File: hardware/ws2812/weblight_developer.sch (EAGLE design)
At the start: 14 parts, among them U1 ATTiny85-20SU

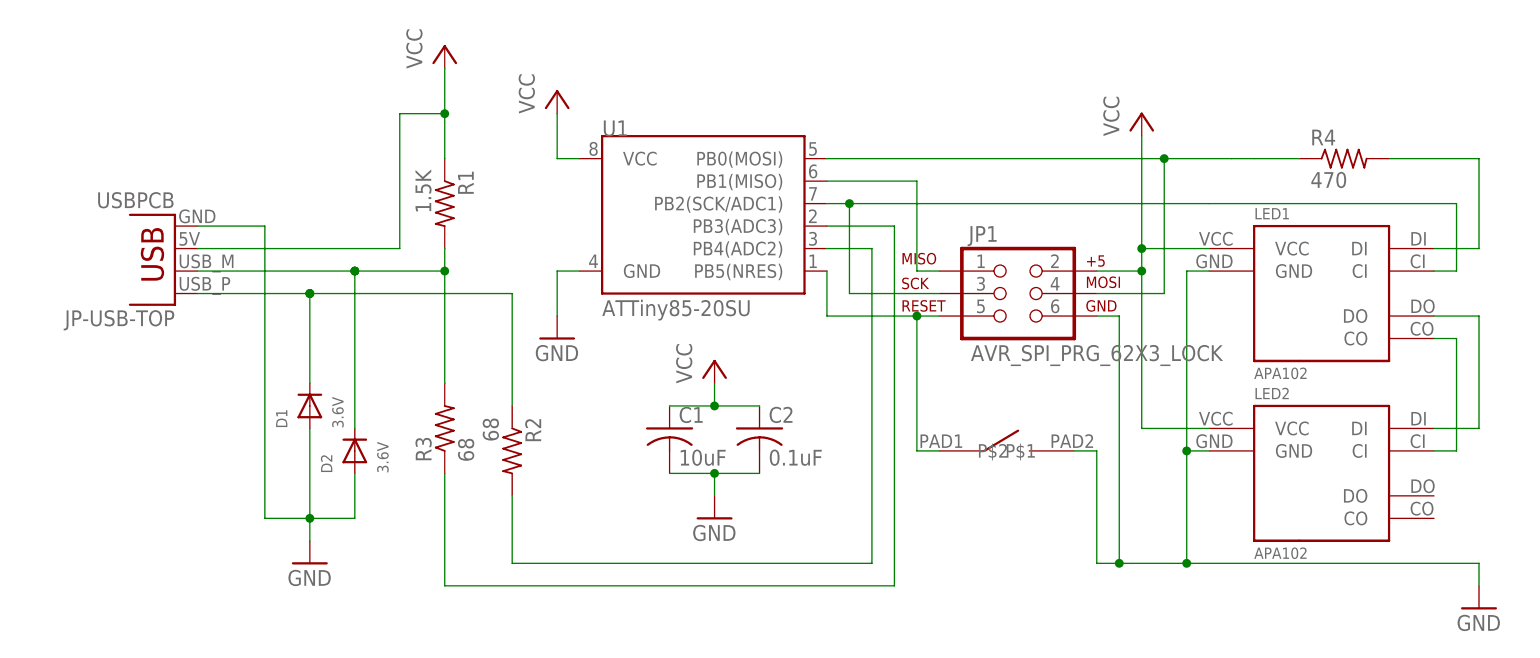
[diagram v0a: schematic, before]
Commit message: Separate LED type and adopt new board versioning scheme
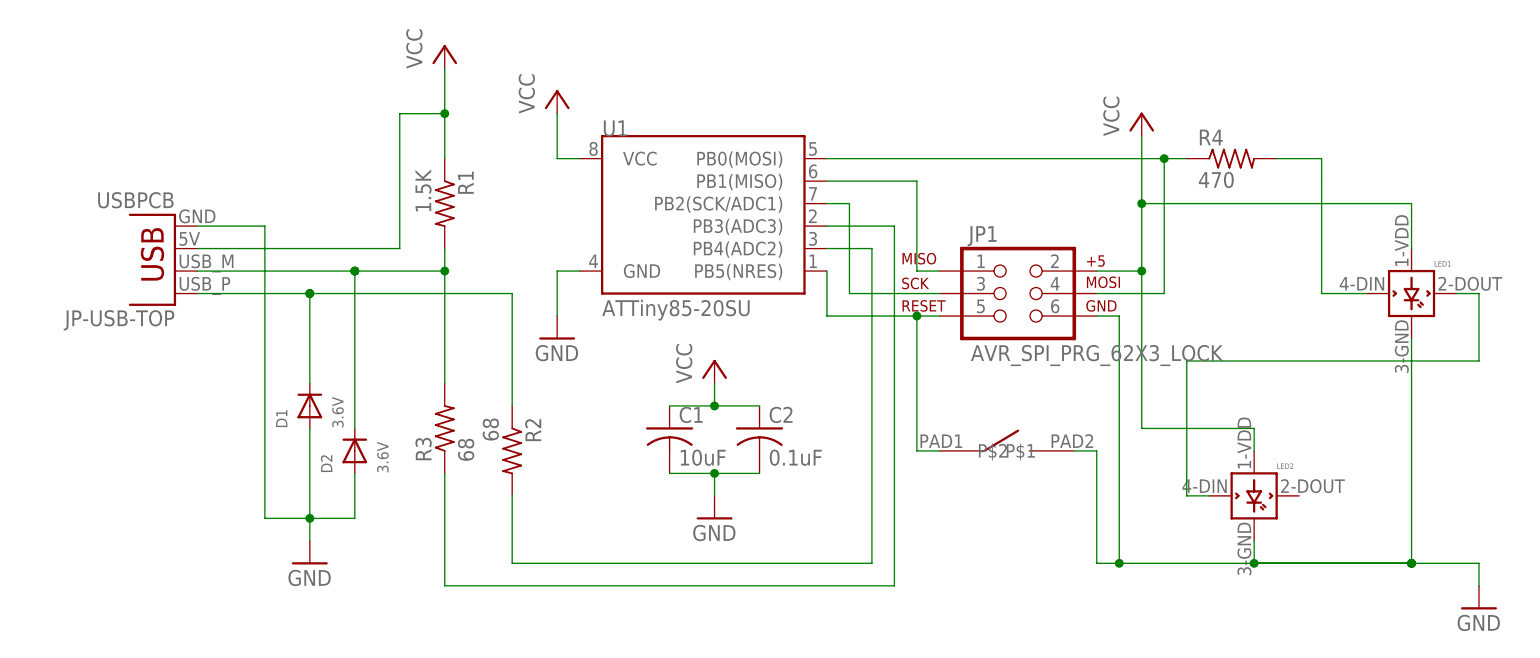
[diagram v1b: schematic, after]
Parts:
- LED1, LED2: value APA102 -> WS2812B; device weblight:APA102 -> weblight:WS2812B
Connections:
- removed net SCK_1: JP1.3, LED1.CI, U1.PB2(SCK/ADC1)
- removed net SCK_2: LED1.CO, LED2.CI
- new net N$4: JP1.3, U1.PB2(SCK/ADC1)
- net DIN_1: now also LED1.DIN; no longer LED1.DI
- net DIN_2: now also LED1.DOUT, LED2.DIN; no longer LED1.DO, LED2.DI
- net VCC: now also LED1.VDD, LED2.VDD; no longer LED1.VCC, LED2.VCC
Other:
- moved on the sheet: R4
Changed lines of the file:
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@@
 <part name="JP1" library="SparkFun-Connectors" deviceset="AVR_SPI_PRG_6" device="2X3_LOCK"/>
 <part name="SW_RESET" library="weblight" deviceset="BUTTON_TD-85XU" device=""/>
-<part name="LED1" library="weblight" deviceset="APA102" device=""/>
-<part name="LED2" library="weblight" deviceset="APA102" device=""/>
+<part name="LED1" library="weblight" deviceset="WS2812B" device=""/>
+<part name="LED2" library="weblight" deviceset="WS2812B" device=""/>
 </parts>
 <sheets>
@@
 <instance part="GND4" gate="1" x="99.06" y="30.48"/>
 <instance part="P+5" gate="VCC" x="60.96" y="86.36"/>
-<instance part="R4" gate="G$1" x="83.82" y="81.28"/>
+<instance part="R4" gate="G$1" x="71.12" y="81.28"/>
 <instance part="JP1" gate="G$1" x="45.72" y="66.04"/>
 <instance part="SW_RESET" gate="G$1" x="45.72" y="48.26"/>
-<instance part="LED1" gate="G$1" x="81.28" y="63.5"/>
-<instance part="LED2" gate="G$1" x="81.28" y="43.18"/>
+<instance part="LED1" gate="G$1" x="91.44" y="66.04"/>
+<instance part="LED2" gate="G$1" x="73.66" y="43.18"/>
 </instances>
 <busses>
@@
 </segment>
 <segment>
-<wire x1="60.96" y1="71.12" x2="68.58" y2="71.12" width="0.1524" layer="91"/>
 <pinref part="P+5" gate="VCC" pin="VCC"/>
 <wire x1="60.96" y1="50.8" x2="60.96" y2="68.58" width="0.1524" layer="91"/>
-<wire x1="60.96" y1="68.58" x2="60.96" y2="71.12" width="0.1524" layer="91"/>
-<wire x1="60.96" y1="83.82" x2="60.96" y2="71.12" width="0.1524" layer="91"/>
-<junction x="60.96" y="71.12"/>
+<wire x1="60.96" y1="68.58" x2="60.96" y2="76.2" width="0.1524" layer="91"/>
+<wire x1="60.96" y1="83.82" x2="60.96" y2="76.2" width="0.1524" layer="91"/>
 <pinref part="JP1" gate="G$1" pin="2"/>
 <wire x1="55.88" y1="68.58" x2="60.96" y2="68.58" width="0.1524" layer="91"/>
 <junction x="60.96" y="68.58"/>
-<pinref part="LED1" gate="G$1" pin="VCC"/>
-<pinref part="LED2" gate="G$1" pin="VCC"/>
-<wire x1="60.96" y1="50.8" x2="68.58" y2="50.8" width="0.1524" layer="91"/>
+<wire x1="60.96" y1="50.8" x2="73.66" y2="50.8" width="0.1524" layer="91"/>
+<pinref part="LED2" gate="G$1" pin="VDD"/>
+<wire x1="73.66" y1="50.8" x2="73.66" y2="48.26" width="0.1524" layer="91"/>
+<pinref part="LED1" gate="G$1" pin="VDD"/>
+<wire x1="91.44" y1="76.2" x2="91.44" y2="71.12" width="0.1524" layer="91"/>
+<wire x1="91.44" y1="76.2" x2="60.96" y2="76.2" width="0.1524" layer="91"/>
+<junction x="60.96" y="76.2"/>
 </segment>
 </net>
@@
 <pinref part="GND4" gate="1" pin="GND"/>
 <wire x1="99.06" y1="35.56" x2="99.06" y2="33.02" width="0.1524" layer="91"/>
-<wire x1="99.06" y1="35.56" x2="66.04" y2="35.56" width="0.1524" layer="91"/>
-<wire x1="66.04" y1="35.56" x2="58.42" y2="35.56" width="0.1524" layer="91"/>
+<wire x1="99.06" y1="35.56" x2="91.44" y2="35.56" width="0.1524" layer="91"/>
+<wire x1="91.44" y1="35.56" x2="73.66" y2="35.56" width="0.1524" layer="91"/>
+<wire x1="73.66" y1="35.56" x2="91.44" y2="35.56" width="0.1524" layer="91"/>
+<wire x1="91.44" y1="35.56" x2="73.66" y2="35.56" width="0.1524" layer="91"/>
+<wire x1="73.66" y1="35.56" x2="58.42" y2="35.56" width="0.1524" layer="91"/>
 <wire x1="58.42" y1="35.56" x2="58.42" y2="63.5" width="0.1524" layer="91"/>
 <pinref part="JP1" gate="G$1" pin="6"/>
@@
 <wire x1="55.88" y1="35.56" x2="58.42" y2="35.56" width="0.1524" layer="91"/>
 <junction x="58.42" y="35.56"/>
+<junction x="91.44" y="35.56"/>
+<junction x="91.44" y="35.56"/>
 <pinref part="LED1" gate="G$1" pin="GND"/>
-<wire x1="68.58" y1="68.58" x2="66.04" y2="68.58" width="0.1524" layer="91"/>
-<wire x1="66.04" y1="68.58" x2="66.04" y2="48.26" width="0.1524" layer="91"/>
-<junction x="66.04" y="35.56"/>
+<wire x1="91.44" y1="35.56" x2="91.44" y2="60.96" width="0.1524" layer="91"/>
 <pinref part="LED2" gate="G$1" pin="GND"/>
-<wire x1="66.04" y1="48.26" x2="66.04" y2="35.56" width="0.1524" layer="91"/>
-<wire x1="66.04" y1="48.26" x2="68.58" y2="48.26" width="0.1524" layer="91"/>
-<junction x="66.04" y="48.26"/>
+<wire x1="73.66" y1="35.56" x2="73.66" y2="38.1" width="0.1524" layer="91"/>
+<junction x="73.66" y="35.56"/>
 </segment>
 <segment>
@@
 <net name="MOSI/DIN_RAW" class="0">
 <segment>
-<wire x1="63.5" y1="81.28" x2="71.12" y2="81.28" width="0.1524" layer="91"/>
-<wire x1="71.12" y1="81.28" x2="73.66" y2="81.28" width="0.1524" layer="91"/>
 <pinref part="R4" gate="G$1" pin="1"/>
-<wire x1="73.66" y1="81.28" x2="78.74" y2="81.28" width="0.1524" layer="91"/>
+<wire x1="63.5" y1="81.28" x2="66.04" y2="81.28" width="0.1524" layer="91"/>
 <wire x1="63.5" y1="81.28" x2="63.5" y2="66.04" width="0.1524" layer="91"/>
 <pinref part="JP1" gate="G$1" pin="4"/>
@@
 <pinref part="JP1" gate="G$1" pin="1"/>
 <wire x1="35.56" y1="68.58" x2="38.1" y2="68.58" width="0.1524" layer="91"/>
-</segment>
-</net>
-<net name="SCK_1" class="0">
-<segment>
-<wire x1="27.94" y1="66.04" x2="27.94" y2="76.2" width="0.1524" layer="91"/>
-<pinref part="U1" gate="G$1" pin="PB2(SCK/ADC1)"/>
-<wire x1="27.94" y1="76.2" x2="25.4" y2="76.2" width="0.1524" layer="91"/>
-<wire x1="27.94" y1="66.04" x2="38.1" y2="66.04" width="0.1524" layer="91"/>
-<pinref part="JP1" gate="G$1" pin="3"/>
-<wire x1="27.94" y1="76.2" x2="68.58" y2="76.2" width="0.1524" layer="91"/>
-<junction x="27.94" y="76.2"/>
-<wire x1="68.58" y1="76.2" x2="96.52" y2="76.2" width="0.1524" layer="91"/>
-<wire x1="96.52" y1="76.2" x2="96.52" y2="68.58" width="0.1524" layer="91"/>
-<pinref part="LED1" gate="G$1" pin="CI"/>
-<wire x1="96.52" y1="68.58" x2="93.98" y2="68.58" width="0.1524" layer="91"/>
 </segment>
 </net>
@@
 <net name="DIN_1" class="0">
 <segment>
-<wire x1="99.06" y1="71.12" x2="93.98" y2="71.12" width="0.1524" layer="91"/>
-<wire x1="99.06" y1="71.12" x2="99.06" y2="81.28" width="0.1524" layer="91"/>
+<pinref part="LED1" gate="G$1" pin="DIN"/>
+<wire x1="81.28" y1="66.04" x2="86.36" y2="66.04" width="0.1524" layer="91"/>
 <pinref part="R4" gate="G$1" pin="2"/>
-<wire x1="99.06" y1="81.28" x2="88.9" y2="81.28" width="0.1524" layer="91"/>
-<pinref part="LED1" gate="G$1" pin="DI"/>
+<wire x1="81.28" y1="66.04" x2="81.28" y2="78.74" width="0.1524" layer="91"/>
+<wire x1="81.28" y1="78.74" x2="81.28" y2="81.28" width="0.1524" layer="91"/>
+<wire x1="81.28" y1="81.28" x2="76.2" y2="81.28" width="0.1524" layer="91"/>
 </segment>
 </net>
 <net name="DIN_2" class="0">
 <segment>
-<pinref part="LED1" gate="G$1" pin="DO"/>
-<wire x1="93.98" y1="63.5" x2="99.06" y2="63.5" width="0.1524" layer="91"/>
-<wire x1="99.06" y1="63.5" x2="99.06" y2="50.8" width="0.1524" layer="91"/>
-<pinref part="LED2" gate="G$1" pin="DI"/>
-<wire x1="99.06" y1="50.8" x2="93.98" y2="50.8" width="0.1524" layer="91"/>
-</segment>
-</net>
-<net name="SCK_2" class="0">
-<segment>
-<pinref part="LED1" gate="G$1" pin="CO"/>
-<wire x1="93.98" y1="60.96" x2="96.52" y2="60.96" width="0.1524" layer="91"/>
-<wire x1="96.52" y1="60.96" x2="96.52" y2="48.26" width="0.1524" layer="91"/>
-<pinref part="LED2" gate="G$1" pin="CI"/>
-<wire x1="96.52" y1="48.26" x2="93.98" y2="48.26" width="0.1524" layer="91"/>
-</segment>
-</net>
+<pinref part="LED1" gate="G$1" pin="DOUT"/>
+<wire x1="96.52" y1="66.04" x2="99.06" y2="66.04" width="0.1524" layer="91"/>
+<wire x1="99.06" y1="66.04" x2="99.06" y2="58.42" width="0.1524" layer="91"/>
+<wire x1="99.06" y1="58.42" x2="66.04" y2="58.42" width="0.1524" layer="91"/>
+<wire x1="66.04" y1="58.42" x2="66.04" y2="43.18" width="0.1524" layer="91"/>
+<pinref part="LED2" gate="G$1" pin="DIN"/>
+<wire x1="66.04" y1="43.18" x2="68.58" y2="43.18" width="0.1524" layer="91"/>
+</segment>
+</net>
+<net name="N$4" class="0">
+<segment>
+<pinref part="JP1" gate="G$1" pin="3"/>
+<pinref part="U1" gate="G$1" pin="PB2(SCK/ADC1)"/>
+<wire x1="27.94" y1="76.2" x2="25.4" y2="76.2" width="0.1524" layer="91"/>
+<wire x1="27.94" y1="66.04" x2="27.94" y2="76.2" width="0.1524" layer="91"/>
+<wire x1="27.94" y1="66.04" x2="38.1" y2="66.04" width="0.1524" layer="91"/>
+</segment>
+</net>
